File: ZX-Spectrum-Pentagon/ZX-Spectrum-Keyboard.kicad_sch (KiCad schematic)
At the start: 140 parts, among them SW1 SW_Push_45deg, SW10 SW_Push_45deg, SW11 SW_Push_45deg, SW12 SW_Push_45deg, SW13 SW_Push_45deg, SW14 SW_Push_45deg, SW15 SW_Push_45deg, SW16 SW_Push_45deg, SW17 SW_Push_45deg, SW18 SW_Push_45deg, SW19 SW_Push_45deg, SW2 SW_Push_45deg, SW20 SW_Push_45deg, SW21 SW_Push_45deg, SW22 SW_Push_45deg, SW23 SW_Push_45deg, SW24 SW_Push_45deg, SW25 SW_Push_45deg, SW26 SW_Push_45deg, SW27 SW_Push_45deg, SW28 SW_Push_45deg, SW29 SW_Push_45deg, SW3 SW_Push_45deg, SW30 SW_Push_45deg, SW31 SW_Push_45deg, SW32 SW_Push_45deg, SW33 SW_Push_45deg, SW34 SW_Push_45deg, SW35 SW_Push_45deg, SW36 SW_Push_45deg, SW37 SW_Push_45deg, SW38 SW_Push_45deg, SW39 SW_Push_45deg, SW4 SW_Push_45deg, SW40 SW_Push_45deg, SW41 SW_Push_45deg, SW42 SW_Push_45deg, SW43 SW_Push_45deg, SW44 SW_Push_45deg, SW45 SW_Push_45deg, SW46 SW_Push_45deg, SW47 SW_Push_45deg, SW48 SW_Push_45deg, SW49 SW_Push_45deg, SW5 SW_Push_45deg, SW50 SW_Push_45deg, SW51 SW_Push_45deg, SW52 SW_Push_45deg, SW53 SW_Push_45deg, SW54 SW_Push_45deg, SW55 SW_Push_45deg, SW56 SW_Push_45deg, SW57 SW_Push_45deg, SW58 SW_Push_45deg, SW59 SW_Push_45deg, SW6 SW_Push_45deg, SW7 SW_Push_45deg, SW8 SW_Push_45deg, SW9 SW_Push_45deg, U1 74HC32, U2 74HC32, U3 74HC32, U4 74HC32, U5 74HC32

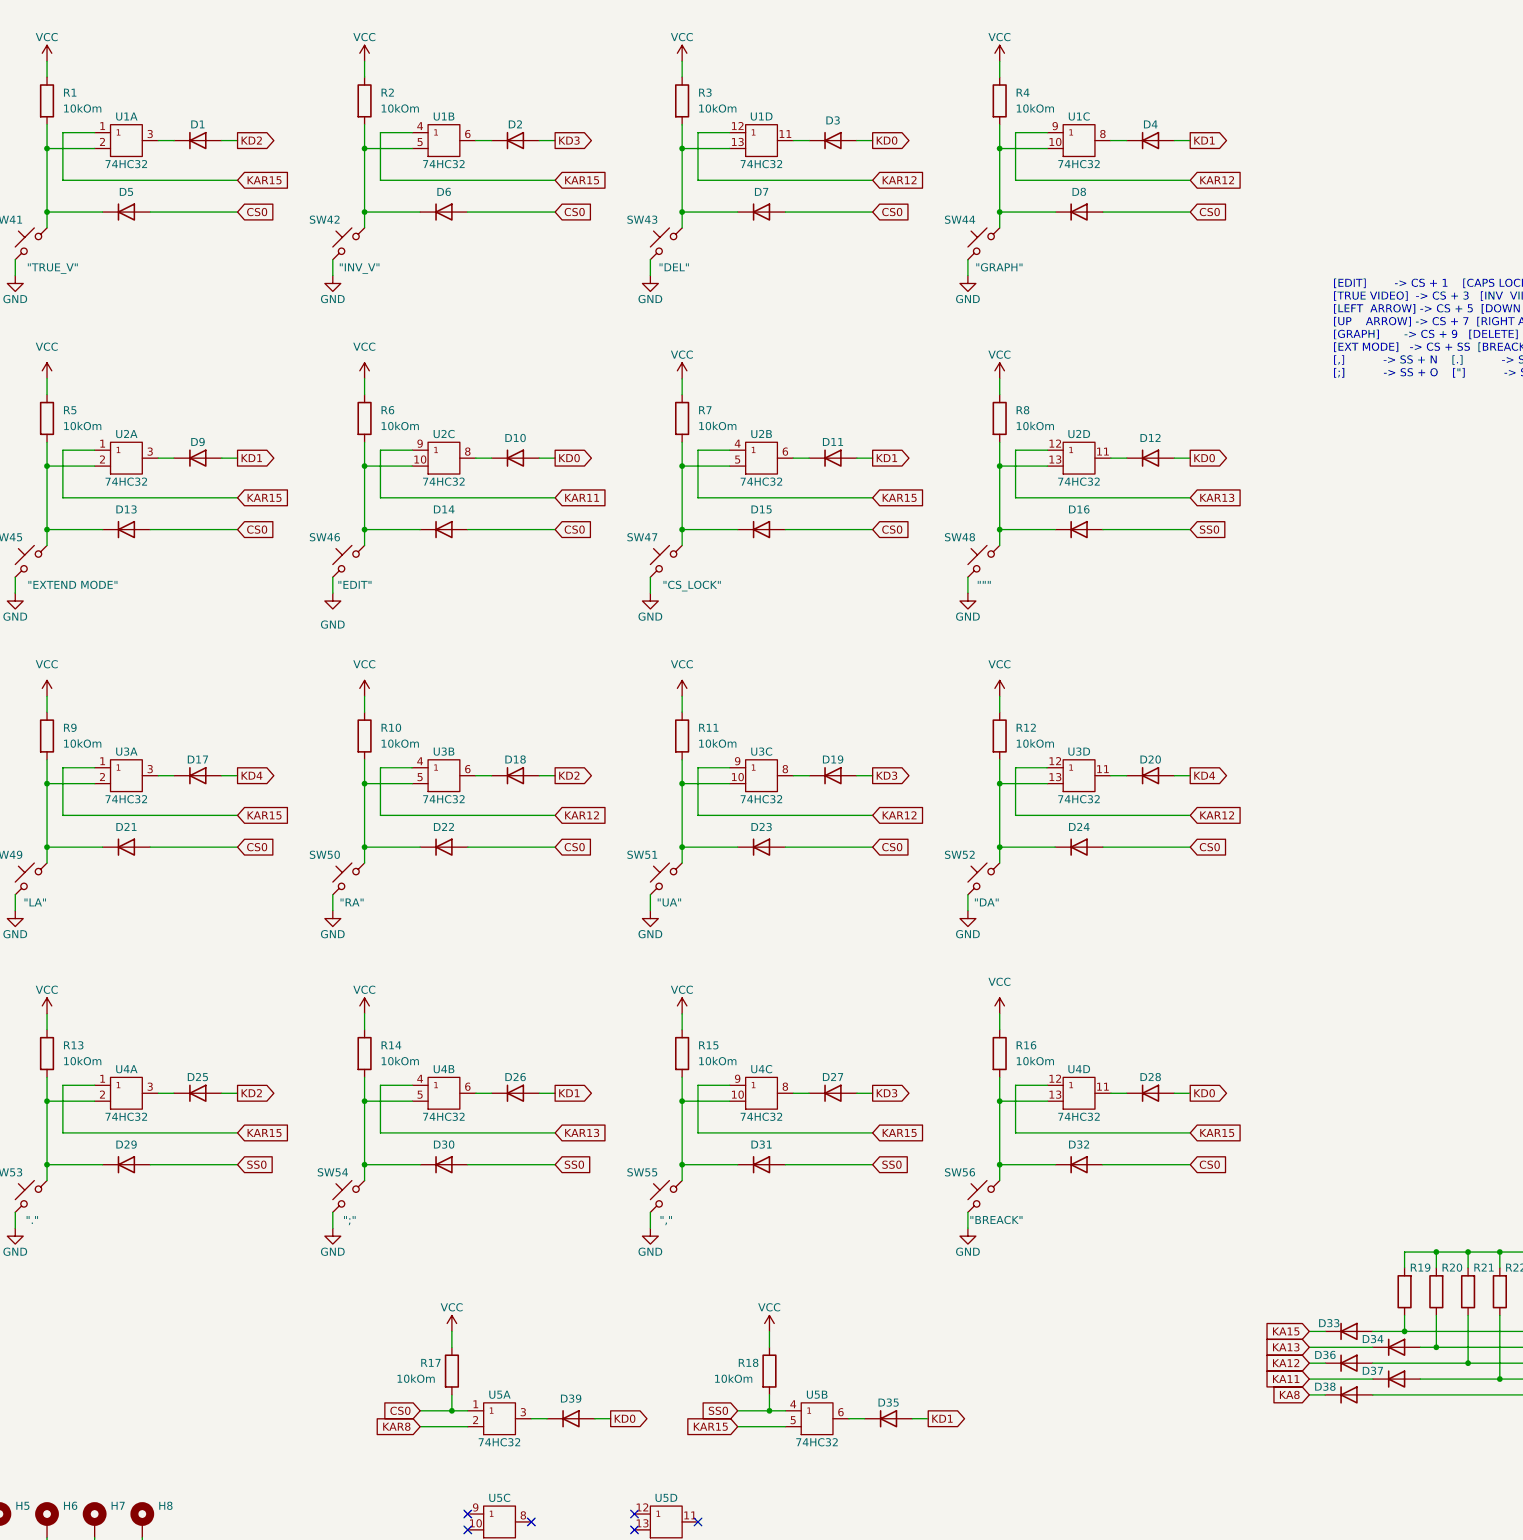
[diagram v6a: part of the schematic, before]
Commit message: migrate ZX-Spectrum-Keyboard to kicad_8.0
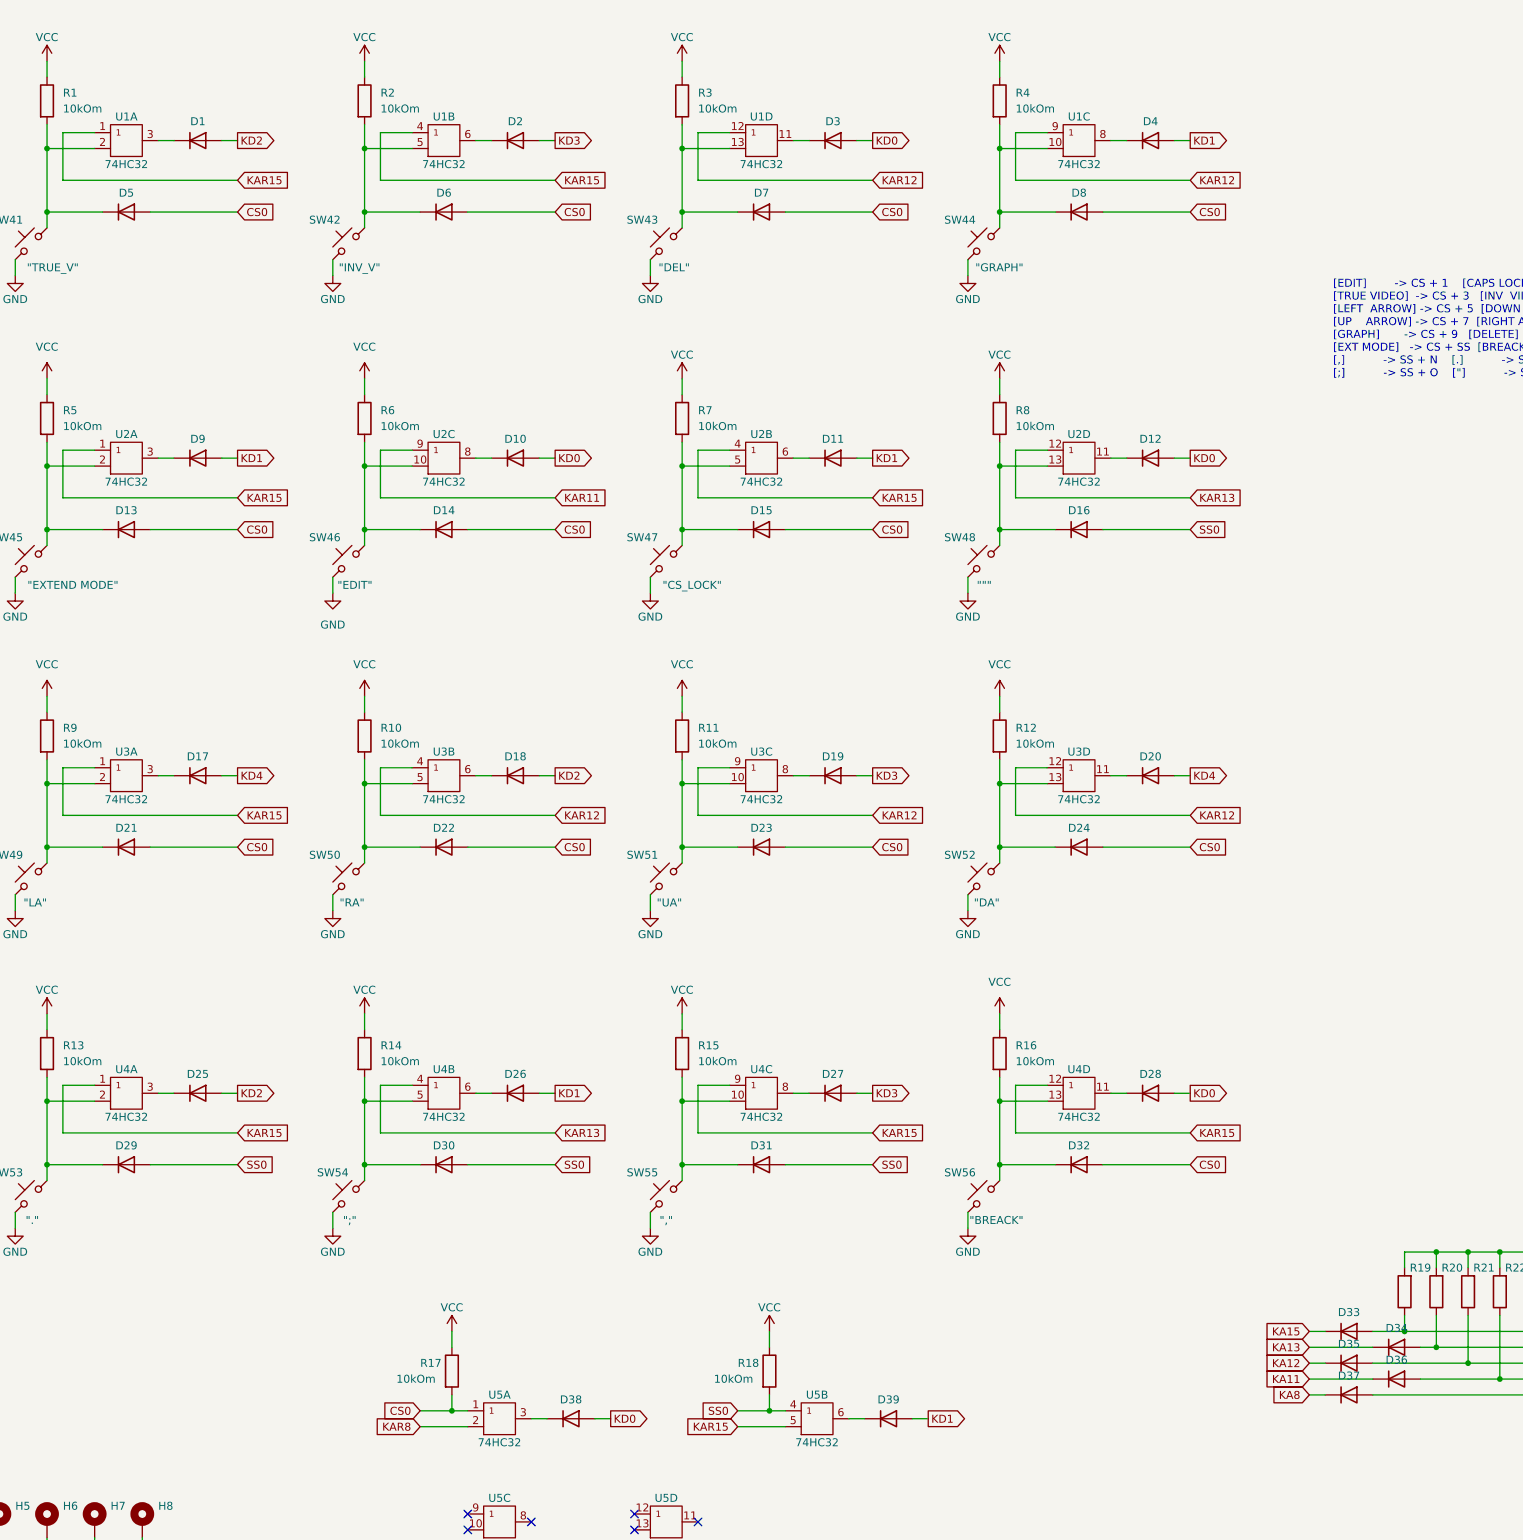
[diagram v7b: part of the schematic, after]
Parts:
- removed D1, D10, D11, D12, D13, D14, D15, D16, D17, D18, D19, D2, D20, D21, D22, D23, D24, D25, D26, D27, D28, D29, D3, D30, D31, D32, D33, D34, D35, D36, D37, D38, D39, D4, D5, D6, D7, D8, D9: 1N4148, Diode_SMD:D_MiniMELF, symbol Simulation_SPICE:DIODE
- added D1, D10, D11, D12, D13, D14, D15, D16, D17, D18, D19, D2, D20, D21, D22, D23, D24, D25, D26, D27, D28, D29, D3, D30, D31, D32, D33, D34, D35, D36, D37, D38, D39, D4, D5, D6, D7, D8, D9: 1N4148, Diode_SMD:D_MiniMELF, symbol Device:D
- JKB1, JKB2: symbol Connector:Conn_01x08_Male -> Connector:Conn_01x08_Pin
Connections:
- net CS0: now also D13.2 (A), D14.2 (A), D15.2 (A), D21.2 (A), D22.2 (A), D23.2 (A), D24.2 (A), D32.2 (A), D5.2 (A), D6.2 (A), D7.2 (A), D8.2 (A)
- net KA11: now also D36.1 (K)
- net KA12: now also D35.1 (K)
- net KA13: now also D34.1 (K)
- net KA15: now also D33.1 (K)
- net KA8: now also D37.1 (K)
- net KAR11: now also D36.2 (A)
- net KAR12: now also D35.2 (A)
- net KAR13: now also D34.2 (A)
- net KAR15: now also D33.2 (A)
- net KAR8: now also D37.2 (A)
- net KD0: now also D10.2 (A), D12.2 (A), D28.2 (A), D3.2 (A), D38.2 (A)
- net KD1: now also D11.2 (A), D26.2 (A), D39.2 (A), D4.2 (A), D9.2 (A)
- net KD2: now also D1.2 (A), D18.2 (A), D25.2 (A)
- net KD3: now also D19.2 (A), D2.2 (A), D27.2 (A)
- net KD4: now also D17.2 (A), D20.2 (A)
- net SS0: now also D16.2 (A), D29.2 (A), D30.2 (A), D31.2 (A)
- net at U3.8 (Y): now also D19.1 (K)
- net at R15.2, SW55.1, U4.10 (B): now also D31.1 (K)
- net at R11.2, SW51.1, U3.10 (B): now also D23.1 (K)
- net at R9.2, SW49.1, U3.2 (B): now also D21.1 (K)
- net at U3.3 (Y): now also D17.1 (K)
- net at R7.2, SW47.1, U2.5 (B): now also D15.1 (K)
- net at R10.2, SW50.1, U3.5 (B): now also D22.1 (K)
- net at R5.2, SW45.1, U2.2 (B): now also D13.1 (K)
- net at R4.2, SW44.1, U1.10 (B): now also D8.1 (K)
- net at R12.2, SW52.1, U3.13 (B): now also D24.1 (K)
- net at R1.2, SW41.1, U1.2 (B): now also D5.1 (K)
- net at U1.3 (Y): now also D1.1 (K)
- net at U1.8 (Y): now also D4.1 (K)
- net at U1.11 (Y): now also D3.1 (K)
- net at R3.2, SW43.1, U1.13 (B): now also D7.1 (K)
- net at U4.3 (Y): now also D25.1 (K)
- net at U2.3 (Y): now also D9.1 (K)
- net at U3.6 (Y): now also D18.1 (K)
- net at R6.2, SW46.1, U2.10 (B): now also D14.1 (K)
- net at R14.2, SW54.1, U4.5 (B): now also D30.1 (K)
- net at U3.11 (Y): now also D20.1 (K)
- net at U4.11 (Y): now also D28.1 (K)
- net at U2.8 (Y): now also D10.1 (K)
- net at U2.11 (Y): now also D12.1 (K)
- net at R8.2, SW48.1, U2.13 (B): now also D16.1 (K)
- net at U5.6 (Y): now also D39.1 (K)
- net at R2.2, SW42.1, U1.5 (B): now also D6.1 (K)
- net at R16.2, SW56.1, U4.13 (B): now also D32.1 (K)
- net at U5.3 (Y): now also D38.1 (K)
- net at R13.2, SW53.1, U4.2 (B): now also D29.1 (K)
- net at U4.8 (Y): now also D27.1 (K)
- net at U4.6 (Y): now also D26.1 (K)
- net at U1.6 (Y): now also D2.1 (K)
- net at U2.6 (Y): now also D11.1 (K)

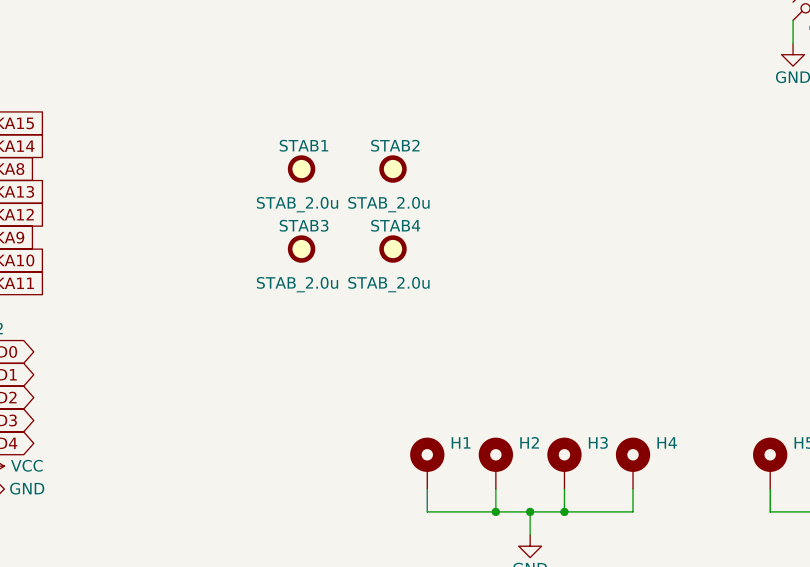
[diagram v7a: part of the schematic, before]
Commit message: update model for ZX-Spectrum-Keyboard & ZX_Keyboard
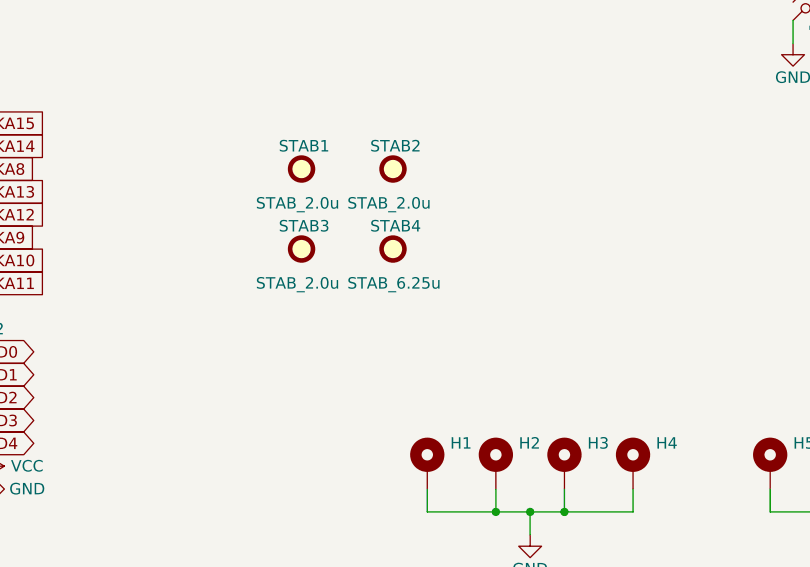
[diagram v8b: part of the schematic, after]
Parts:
- STAB4: value STAB_2.0u -> STAB_6.25u
